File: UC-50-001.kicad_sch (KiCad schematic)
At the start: 0 parts

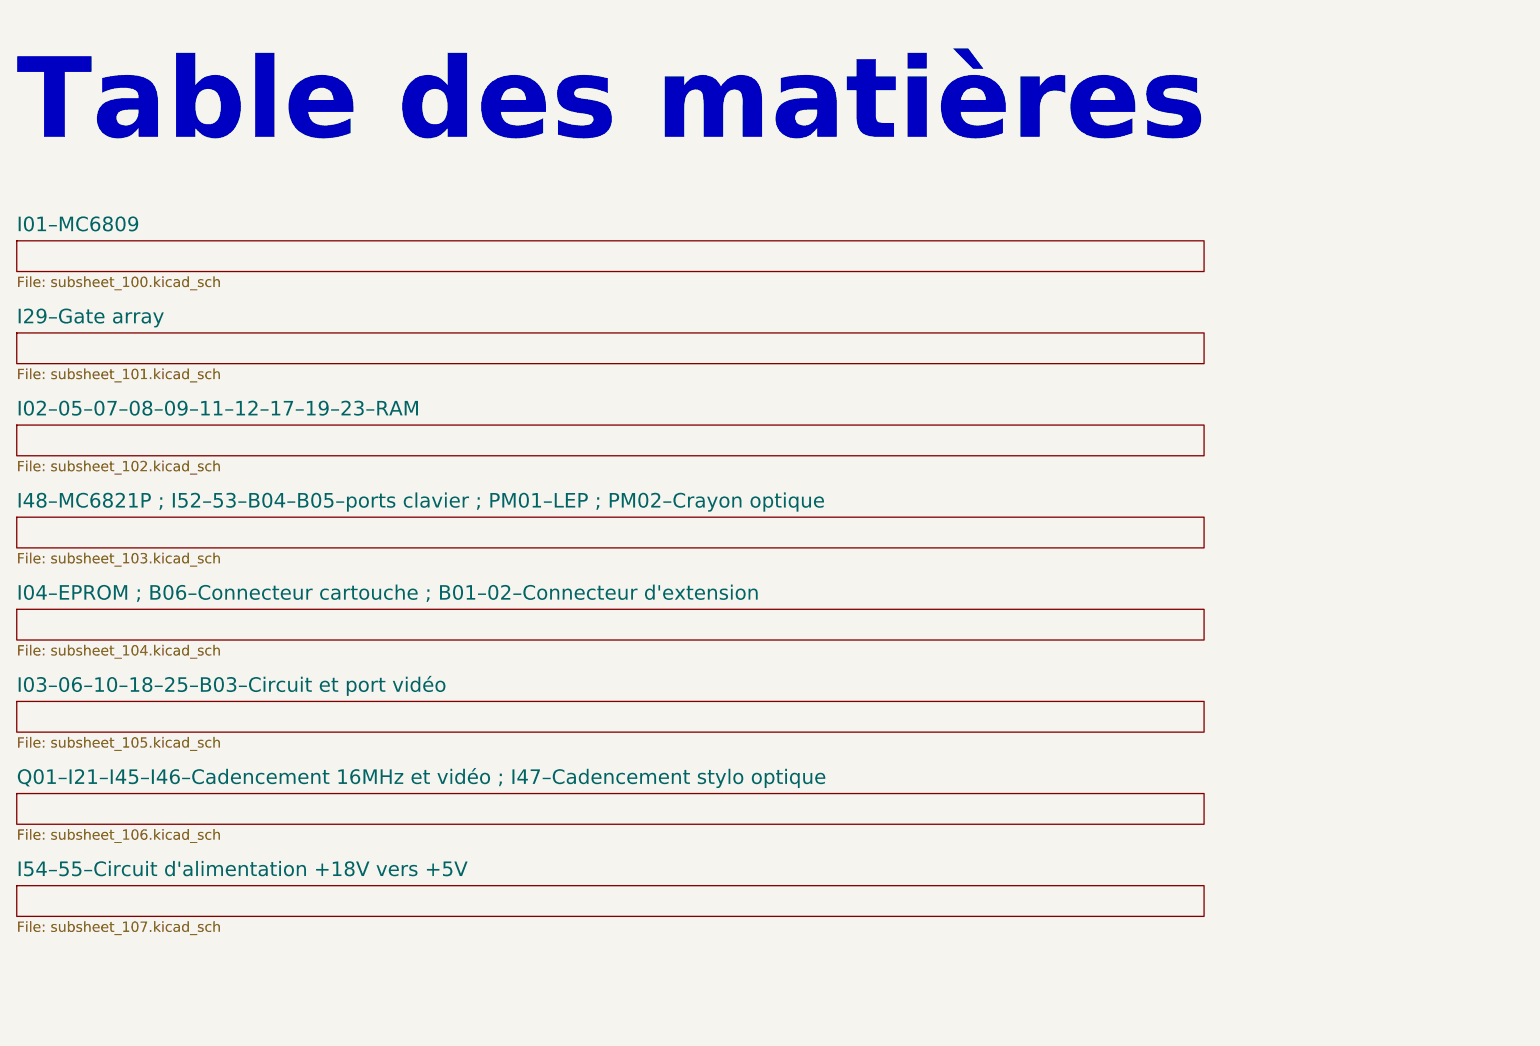
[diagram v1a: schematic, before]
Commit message: decodage d'addresse, re-pagination
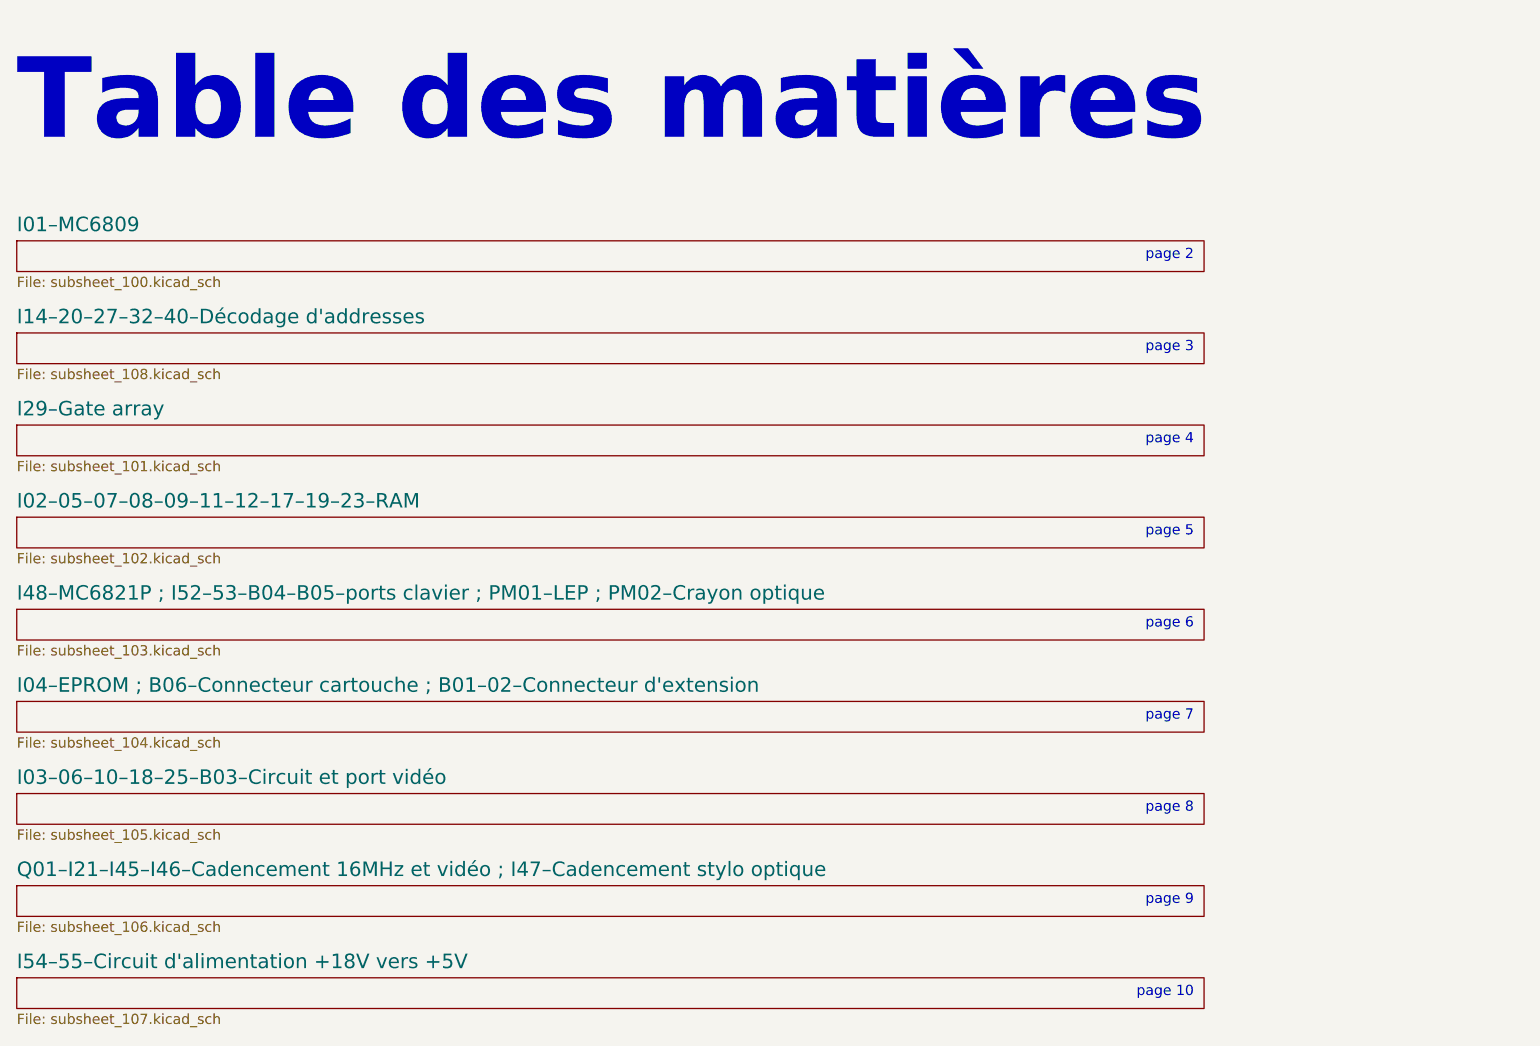
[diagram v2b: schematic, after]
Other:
- added sheet I14–20–27–32–40–Décodage d'addresses (subsheet_108.kicad_sch)
- note added: "page 10"
- note added: "page 2"
- note added: "page 3"
- note added: "page 4"
- note added: "page 5"
- note added: "page 6"
- note added: "page 7"
- note added: "page 8"
- note added: "page 9"

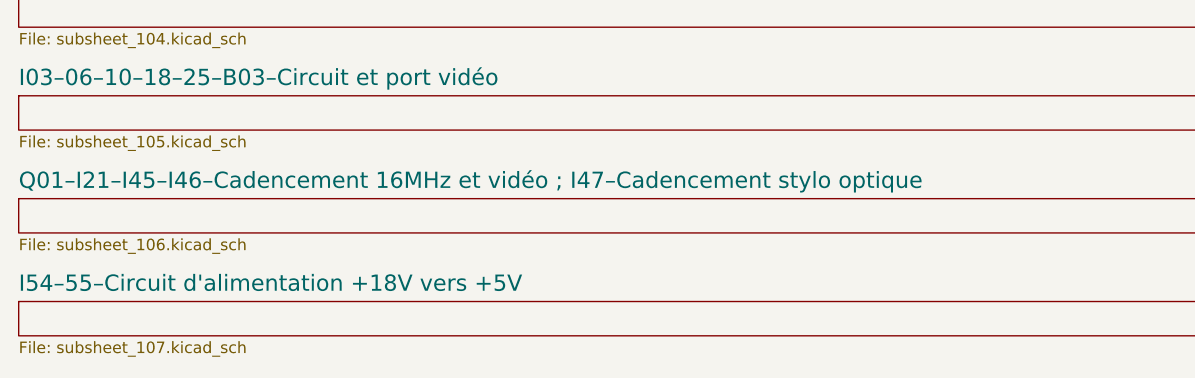
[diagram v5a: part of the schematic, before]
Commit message: schematic : mounting holes
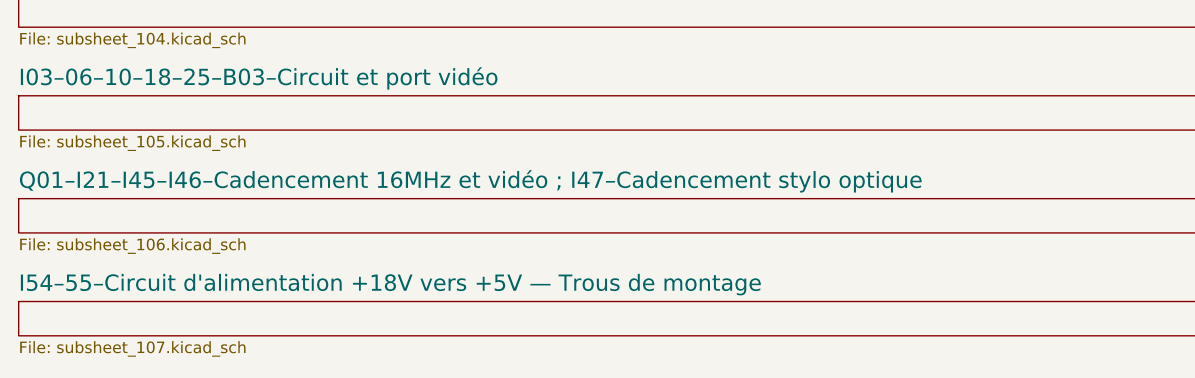
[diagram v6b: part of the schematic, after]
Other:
- sheet I54–55–Circuit d'alimentation +18V vers +5V renamed I54–55–Circuit d'alimentation +18V vers +5V — Trous de montage
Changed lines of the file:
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@@
     (stroke (width 0.1524) (type solid) (color 0 0 0 0))
     (fill (color 0 0 0 0.0000))
-    (property "Sheet name" "I54–55–Circuit d'alimentation +18V vers +5V" (id 0) (at 30.48 145.0734 0)
+    (property "Sheet name" "I54–55–Circuit d'alimentation +18V vers +5V — Trous de montage" (id 0) (at 30.48 145.0734 0)
       (effects (font (size 1.8 1.8)) (justify left bottom))
     )
@@
       (reference "D08") (unit 1) (value "?? 1N4148") (footprint "")
     )
+    (path "/86f44e2a-9fb4-43d0-b64c-d20135fe820e/da429d6e-09f9-4359-87f0-5986ac9e08cb"
+      (reference "H1") (unit 1) (value "3,5 mm") (footprint "mounting-holes-mo5:MountingHole_3.5mm_limited_courtyard")
+    )
+    (path "/86f44e2a-9fb4-43d0-b64c-d20135fe820e/e844089c-2f6d-44bc-b975-b8b654fb2774"
+      (reference "H2") (unit 1) (value "3,5 mm") (footprint "mounting-holes-mo5:MountingHole_3.5mm_limited_courtyard")
+    )
+    (path "/86f44e2a-9fb4-43d0-b64c-d20135fe820e/6cedb50b-7a38-410d-ad59-12572281bebc"
+      (reference "H3") (unit 1) (value "4 mm") (footprint "mounting-holes-mo5:MountingHole_4mm_limited_courtyard")
+    )
+    (path "/86f44e2a-9fb4-43d0-b64c-d20135fe820e/94adfc7e-f979-4958-9a9b-251aee8c3276"
+      (reference "H4") (unit 1) (value "4 mm") (footprint "mounting-holes-mo5:MountingHole_4mm_limited_courtyard")
+    )
+    (path "/86f44e2a-9fb4-43d0-b64c-d20135fe820e/09a1a547-1d52-4c98-9378-410ccbcc9554"
+      (reference "H5") (unit 1) (value "4 mm") (footprint "mounting-holes-mo5:MountingHole_4mm_limited_courtyard")
+    )
+    (path "/86f44e2a-9fb4-43d0-b64c-d20135fe820e/331cc9d3-6c87-4928-92a7-2c4f9e7a5841"
+      (reference "H6") (unit 1) (value "4 mm") (footprint "mounting-holes-mo5:MountingHole_4mm_limited_courtyard")
+    )
+    (path "/86f44e2a-9fb4-43d0-b64c-d20135fe820e/453cd238-dd99-4433-92d7-b7ebfaa87a6b"
+      (reference "H7") (unit 1) (value "8,8 mm") (footprint "mounting-holes-mo5:MountingHole_8.8mm_limited_courtyard")
+    )
+    (path "/86f44e2a-9fb4-43d0-b64c-d20135fe820e/9b905902-827e-455d-8a70-6c0832fbc729"
+      (reference "H8") (unit 1) (value "8,8 mm") (footprint "mounting-holes-mo5:MountingHole_8.8mm_limited_courtyard")
+    )
     (path "/afd59d07-bfd6-4bc9-8176-e0ddec1872a1/63085d07-f111-48f0-9996-774660e796f0"
